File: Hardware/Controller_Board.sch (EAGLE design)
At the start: 19 parts, among them Q7 3.6864MHz, U1 ATMEGA328P-PU, U2 REF3020AIDBZT

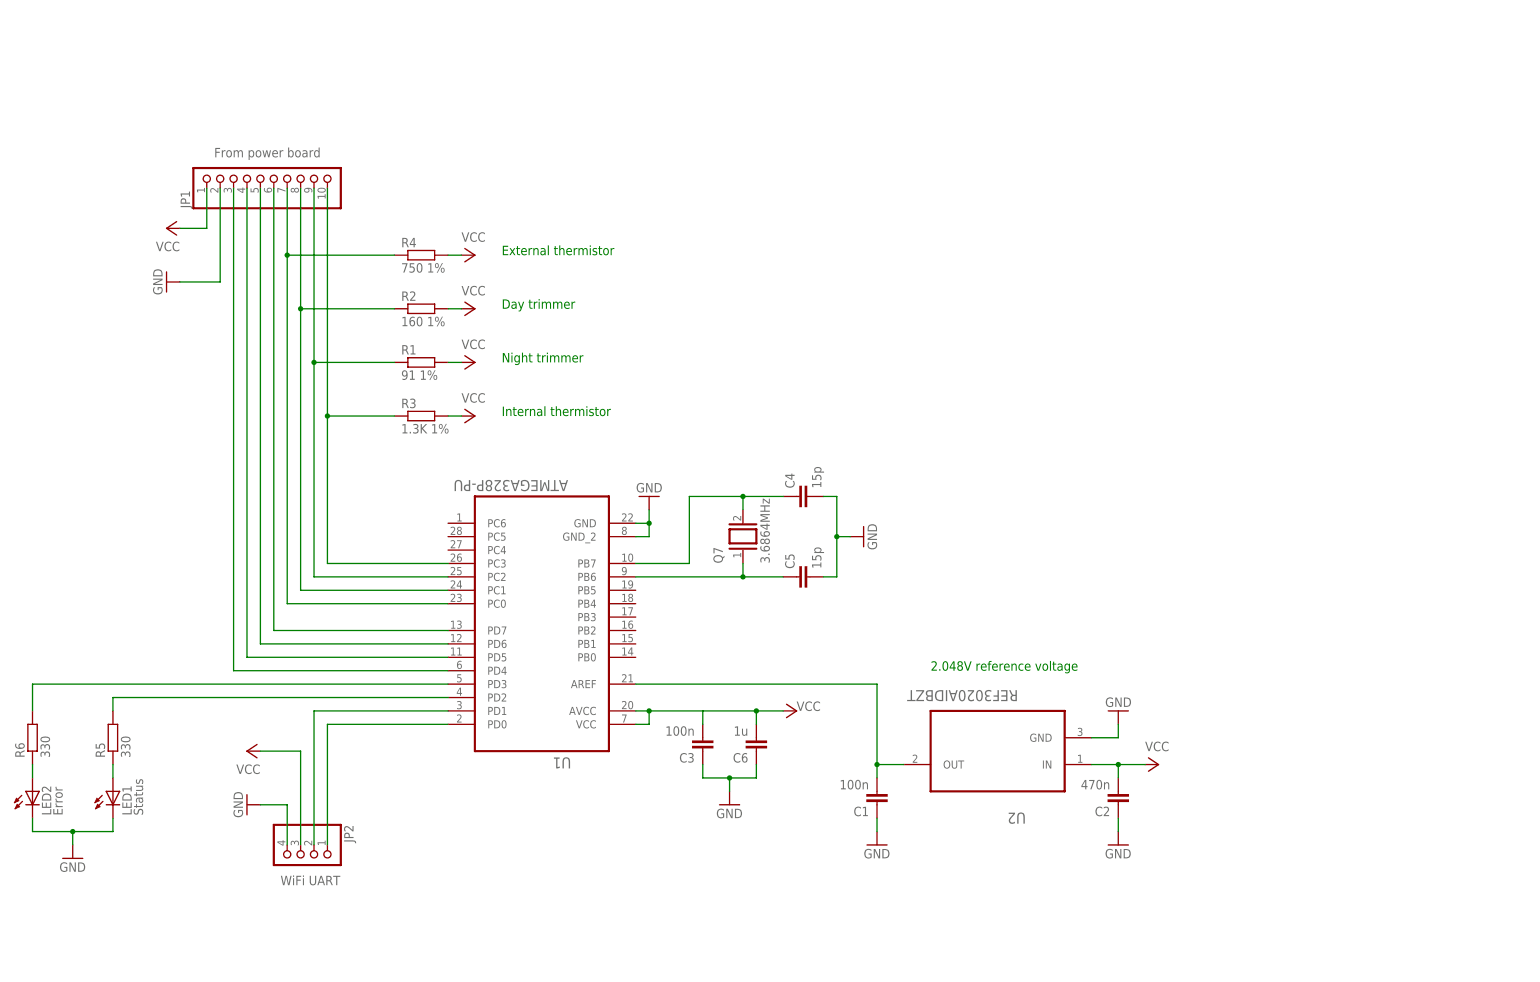
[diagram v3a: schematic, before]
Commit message: Added spare leds and connector to the controller board. Components could be populated if needed.
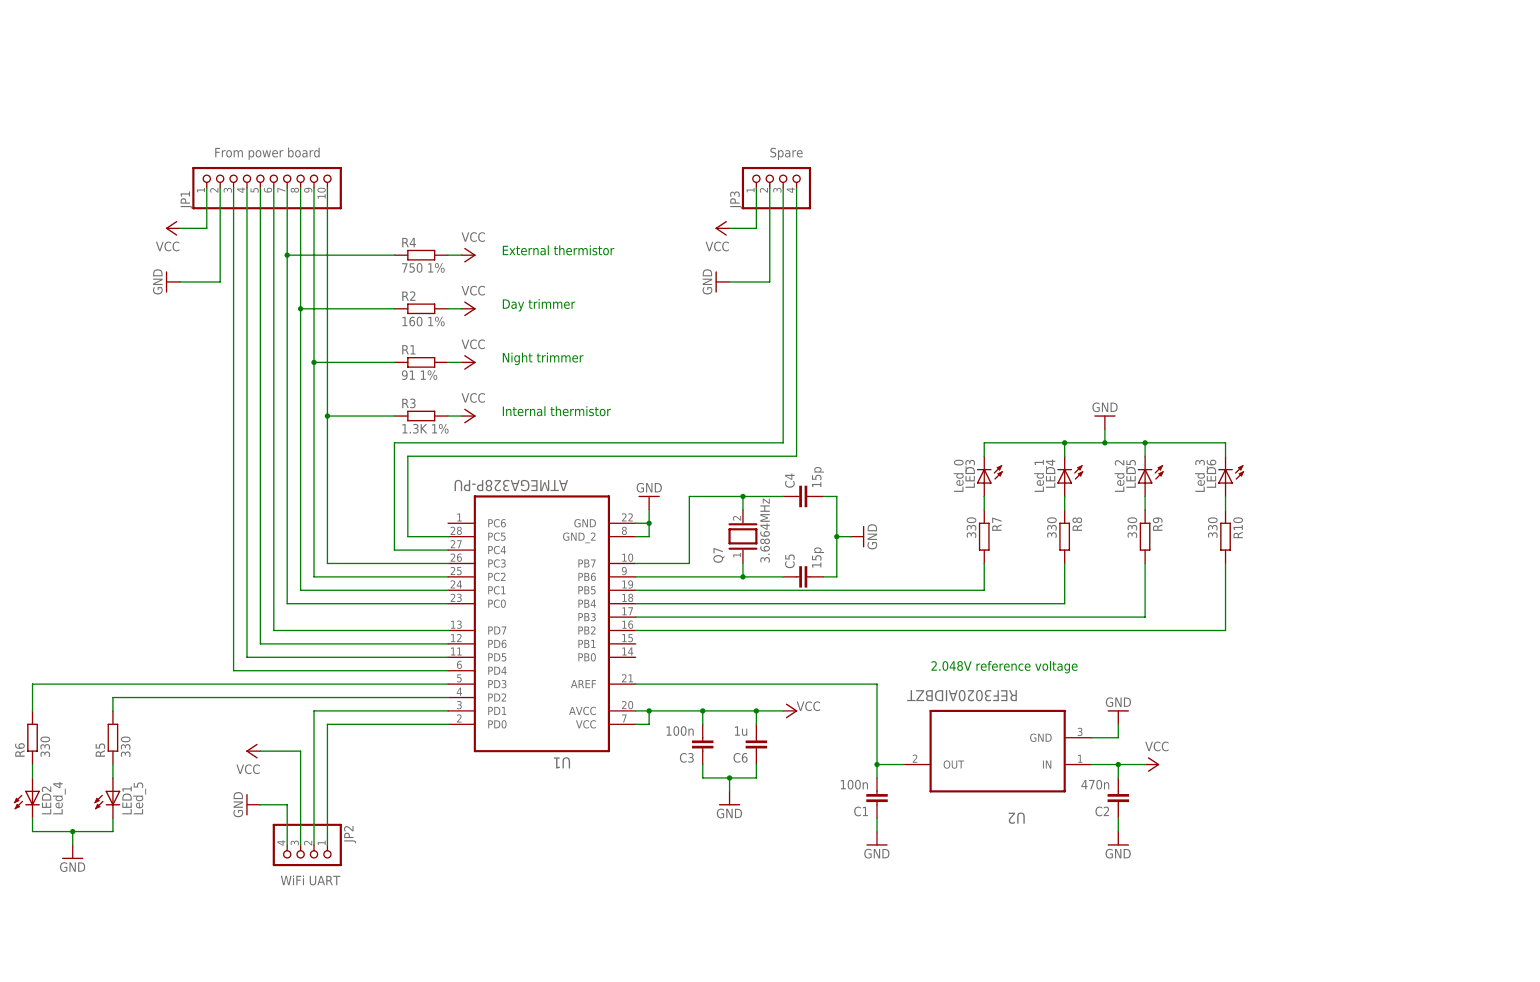
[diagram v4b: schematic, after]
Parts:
- added JP3: Spare, pinhead:PINHD-1X4
- added LED3: Led_0, led:LED5MM
- added LED4: Led_1, led:LED5MM
- added LED5: Led_2, led:LED5MM
- added LED6: Led_3, led:LED5MM
- added R10, R7, R8, R9: 330, resistor:R-EU_0207/10
- LED1: value Status -> Led_5
- LED2: value Error -> Led_4
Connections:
- new net N$15: LED3.A, R7.1
- new net N$17: LED4.A, R8.1
- new net N$18: R8.2, U1.PB4
- new net N$19: R7.2, U1.PB5
- new net N$20: JP3.3, U1.PC4
- new net N$21: LED5.A, R9.1
- new net N$22: R9.2, U1.PB3
- new net N$23: JP3.4, U1.PC5
- new net N$24: LED6.A, R10.1
- new net N$25: R10.2, U1.PB2
- net GND: now also JP3.2, LED3.C, LED4.C, LED5.C, LED6.C
- net VCC: now also JP3.1
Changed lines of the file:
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@@
 <setting verticaltext="down"/>
 </settings>
-<grid distance="0.1" unitdist="inch" unit="inch" style="dots" multiple="1" display="yes" altdistance="0.01" altunitdist="inch" altunit="inch"/>
+<grid distance="0.1" unitdist="inch" unit="inch" style="lines" multiple="1" display="yes" altdistance="0.01" altunitdist="inch" altunit="inch"/>
 <layers>
 <layer number="1" name="Top" color="4" fill="1" visible="no" active="no"/>
@@
 <part name="GND2" library="supply1" deviceset="GND" device=""/>
 <part name="P+7" library="supply1" deviceset="VCC" device=""/>
-<part name="LED1" library="led" deviceset="LED" device="5MM" value="Status"/>
+<part name="LED1" library="led" deviceset="LED" device="5MM" value="Led_5"/>
 <part name="GND3" library="supply1" deviceset="GND" device=""/>
 <part name="R5" library="resistor" deviceset="R-EU_" device="0207/10" value="330"/>
 <part name="C6" library="rcl" deviceset="C-EU" device="050-035X075" value="1u"/>
-<part name="LED2" library="led" deviceset="LED" device="5MM" value="Error"/>
+<part name="LED2" library="led" deviceset="LED" device="5MM" value="Led_4"/>
 <part name="R6" library="resistor" deviceset="R-EU_" device="0207/10" value="330"/>
+<part name="LED3" library="led" deviceset="LED" device="5MM" value="Led_0"/>
+<part name="GND5" library="supply1" deviceset="GND" device=""/>
+<part name="R7" library="resistor" deviceset="R-EU_" device="0207/10" value="330"/>
+<part name="LED4" library="led" deviceset="LED" device="5MM" value="Led_1"/>
+<part name="R8" library="resistor" deviceset="R-EU_" device="0207/10" value="330"/>
+<part name="LED5" library="led" deviceset="LED" device="5MM" value="Led_2"/>
+<part name="R9" library="resistor" deviceset="R-EU_" device="0207/10" value="330"/>
+<part name="LED6" library="led" deviceset="LED" device="5MM" value="Led_3"/>
+<part name="R10" library="resistor" deviceset="R-EU_" device="0207/10" value="330"/>
+<part name="JP3" library="pinhead" deviceset="PINHD-1X4" device="" value="Spare"/>
+<part name="P+8" library="supply1" deviceset="VCC" device=""/>
+<part name="GND7" library="supply1" deviceset="GND" device=""/>
 </parts>
 <sheets>
@@
 <instance part="LED2" gate="G$1" x="-43.18" y="127"/>
 <instance part="R6" gate="G$1" x="-43.18" y="137.16" rot="R90"/>
+<instance part="LED3" gate="G$1" x="137.16" y="185.42" rot="R180"/>
+<instance part="GND5" gate="1" x="160.02" y="198.12" rot="R180"/>
+<instance part="R7" gate="G$1" x="137.16" y="175.26" rot="R270"/>
+<instance part="LED4" gate="G$1" x="152.4" y="185.42" rot="R180"/>
+<instance part="R8" gate="G$1" x="152.4" y="175.26" rot="R270"/>
+<instance part="LED5" gate="G$1" x="167.64" y="185.42" rot="R180"/>
+<instance part="R9" gate="G$1" x="167.64" y="175.26" rot="R270"/>
+<instance part="LED6" gate="G$1" x="182.88" y="185.42" rot="R180"/>
+<instance part="R10" gate="G$1" x="182.88" y="175.26" rot="R270"/>
+<instance part="JP3" gate="A" x="99.06" y="243.84" smashed="yes" rot="R90">
+<attribute name="NAME" x="90.805" y="237.49" size="1.778" layer="95" rot="R90"/>
+<attribute name="VALUE" x="102.87" y="248.92" size="1.778" layer="96" rot="R180"/>
+</instance>
+<instance part="P+8" gate="VCC" x="86.36" y="233.68" rot="R90"/>
+<instance part="GND7" gate="1" x="86.36" y="223.52" rot="R270"/>
 </instances>
 <busses>
@@
 <junction x="-35.56" y="119.38"/>
 </segment>
+<segment>
+<pinref part="LED5" gate="G$1" pin="C"/>
+<wire x1="167.64" y1="190.5" x2="167.64" y2="193.04" width="0.1524" layer="91"/>
+<wire x1="167.64" y1="193.04" x2="160.02" y2="193.04" width="0.1524" layer="91"/>
+<pinref part="GND5" gate="1" pin="GND"/>
+<wire x1="160.02" y1="193.04" x2="152.4" y2="193.04" width="0.1524" layer="91"/>
+<wire x1="160.02" y1="195.58" x2="160.02" y2="193.04" width="0.1524" layer="91"/>
+<pinref part="LED4" gate="G$1" pin="C"/>
+<wire x1="152.4" y1="190.5" x2="152.4" y2="193.04" width="0.1524" layer="91"/>
+<pinref part="LED3" gate="G$1" pin="C"/>
+<wire x1="152.4" y1="193.04" x2="137.16" y2="193.04" width="0.1524" layer="91"/>
+<wire x1="137.16" y1="193.04" x2="137.16" y2="190.5" width="0.1524" layer="91"/>
+<junction x="152.4" y="193.04"/>
+<junction x="160.02" y="193.04"/>
+<pinref part="LED6" gate="G$1" pin="C"/>
+<wire x1="182.88" y1="190.5" x2="182.88" y2="193.04" width="0.1524" layer="91"/>
+<wire x1="182.88" y1="193.04" x2="167.64" y2="193.04" width="0.1524" layer="91"/>
+<junction x="167.64" y="193.04"/>
+</segment>
+<segment>
+<pinref part="GND7" gate="1" pin="GND"/>
+<wire x1="88.9" y1="223.52" x2="96.52" y2="223.52" width="0.1524" layer="91"/>
+<pinref part="JP3" gate="A" pin="2"/>
+<wire x1="96.52" y1="223.52" x2="96.52" y2="241.3" width="0.1524" layer="91"/>
+</segment>
 </net>
 <net name="VCC" class="0">
@@
 </segment>
 <segment>
-<pinref part="U2" gate="A" pin="IN"/>
-<wire x1="157.48" y1="132.08" x2="162.56" y2="132.08" width="0.1524" layer="91"/>
 <pinref part="C2" gate="G$1" pin="2"/>
 <wire x1="162.56" y1="132.08" x2="162.56" y2="129.54" width="0.1524" layer="91"/>
-<junction x="162.56" y="132.08"/>
 <wire x1="162.56" y1="132.08" x2="167.64" y2="132.08" width="0.1524" layer="91"/>
 <pinref part="P+4" gate="VCC" pin="VCC"/>
+<pinref part="U2" gate="A" pin="IN"/>
+<wire x1="162.56" y1="132.08" x2="157.48" y2="132.08" width="0.1524" layer="91"/>
+<junction x="162.56" y="132.08"/>
 </segment>
 <segment>
@@
 <wire x1="83.82" y1="142.24" x2="73.66" y2="142.24" width="0.1524" layer="91"/>
 <junction x="73.66" y="142.24"/>
+<junction x="83.82" y="142.24"/>
 </segment>
 <segment>
@@
 <wire x1="0" y1="134.62" x2="7.62" y2="134.62" width="0.1524" layer="91"/>
 <wire x1="7.62" y1="134.62" x2="7.62" y2="116.84" width="0.1524" layer="91"/>
+</segment>
+<segment>
+<pinref part="P+8" gate="VCC" pin="VCC"/>
+<wire x1="88.9" y1="233.68" x2="93.98" y2="233.68" width="0.1524" layer="91"/>
+<pinref part="JP3" gate="A" pin="1"/>
+<wire x1="93.98" y1="233.68" x2="93.98" y2="241.3" width="0.1524" layer="91"/>
 </segment>
 </net>
@@
 </segment>
 </net>
+<net name="N$15" class="0">
+<segment>
+<pinref part="R7" gate="G$1" pin="1"/>
+<pinref part="LED3" gate="G$1" pin="A"/>
+<wire x1="137.16" y1="180.34" x2="137.16" y2="182.88" width="0.1524" layer="91"/>
+</segment>
+</net>
+<net name="N$17" class="0">
+<segment>
+<pinref part="R8" gate="G$1" pin="1"/>
+<pinref part="LED4" gate="G$1" pin="A"/>
+<wire x1="152.4" y1="180.34" x2="152.4" y2="182.88" width="0.1524" layer="91"/>
+</segment>
+</net>
+<net name="N$18" class="0">
+<segment>
+<pinref part="R8" gate="G$1" pin="2"/>
+<wire x1="152.4" y1="162.56" x2="152.4" y2="170.18" width="0.1524" layer="91"/>
+<pinref part="U1" gate="A" pin="PB4"/>
+<wire x1="71.12" y1="162.56" x2="152.4" y2="162.56" width="0.1524" layer="91"/>
+</segment>
+</net>
+<net name="N$19" class="0">
+<segment>
+<pinref part="R7" gate="G$1" pin="2"/>
+<pinref part="U1" gate="A" pin="PB5"/>
+<wire x1="71.12" y1="165.1" x2="137.16" y2="165.1" width="0.1524" layer="91"/>
+<wire x1="137.16" y1="165.1" x2="137.16" y2="170.18" width="0.1524" layer="91"/>
+</segment>
+</net>
+<net name="N$21" class="0">
+<segment>
+<pinref part="R9" gate="G$1" pin="1"/>
+<pinref part="LED5" gate="G$1" pin="A"/>
+<wire x1="167.64" y1="180.34" x2="167.64" y2="182.88" width="0.1524" layer="91"/>
+</segment>
+</net>
+<net name="N$22" class="0">
+<segment>
+<pinref part="R9" gate="G$1" pin="2"/>
+<pinref part="U1" gate="A" pin="PB3"/>
+<wire x1="71.12" y1="160.02" x2="167.64" y2="160.02" width="0.1524" layer="91"/>
+<wire x1="167.64" y1="160.02" x2="167.64" y2="170.18" width="0.1524" layer="91"/>
+</segment>
+</net>
+<net name="N$24" class="0">
+<segment>
+<pinref part="R10" gate="G$1" pin="1"/>
+<pinref part="LED6" gate="G$1" pin="A"/>
+<wire x1="182.88" y1="180.34" x2="182.88" y2="182.88" width="0.1524" layer="91"/>
+</segment>
+</net>
+<net name="N$25" class="0">
+<segment>
+<pinref part="R10" gate="G$1" pin="2"/>
+<pinref part="U1" gate="A" pin="PB2"/>
+<wire x1="71.12" y1="157.48" x2="182.88" y2="157.48" width="0.1524" layer="91"/>
+<wire x1="182.88" y1="157.48" x2="182.88" y2="170.18" width="0.1524" layer="91"/>
+</segment>
+</net>
+<net name="N$20" class="0">
+<segment>
+<pinref part="JP3" gate="A" pin="3"/>
+<wire x1="99.06" y1="241.3" x2="99.06" y2="193.04" width="0.1524" layer="91"/>
+<wire x1="99.06" y1="193.04" x2="25.4" y2="193.04" width="0.1524" layer="91"/>
+<wire x1="25.4" y1="193.04" x2="25.4" y2="172.72" width="0.1524" layer="91"/>
+<pinref part="U1" gate="A" pin="PC4"/>
+<wire x1="25.4" y1="172.72" x2="35.56" y2="172.72" width="0.1524" layer="91"/>
+</segment>
+</net>
+<net name="N$23" class="0">
+<segment>
+<pinref part="U1" gate="A" pin="PC5"/>
+<wire x1="35.56" y1="175.26" x2="27.94" y2="175.26" width="0.1524" layer="91"/>
+<wire x1="27.94" y1="175.26" x2="27.94" y2="190.5" width="0.1524" layer="91"/>
+<wire x1="27.94" y1="190.5" x2="101.6" y2="190.5" width="0.1524" layer="91"/>
+<pinref part="JP3" gate="A" pin="4"/>
+<wire x1="101.6" y1="190.5" x2="101.6" y2="241.3" width="0.1524" layer="91"/>
+</segment>
+</net>

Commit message: Added microcontroller SPI programming header to the controller board.
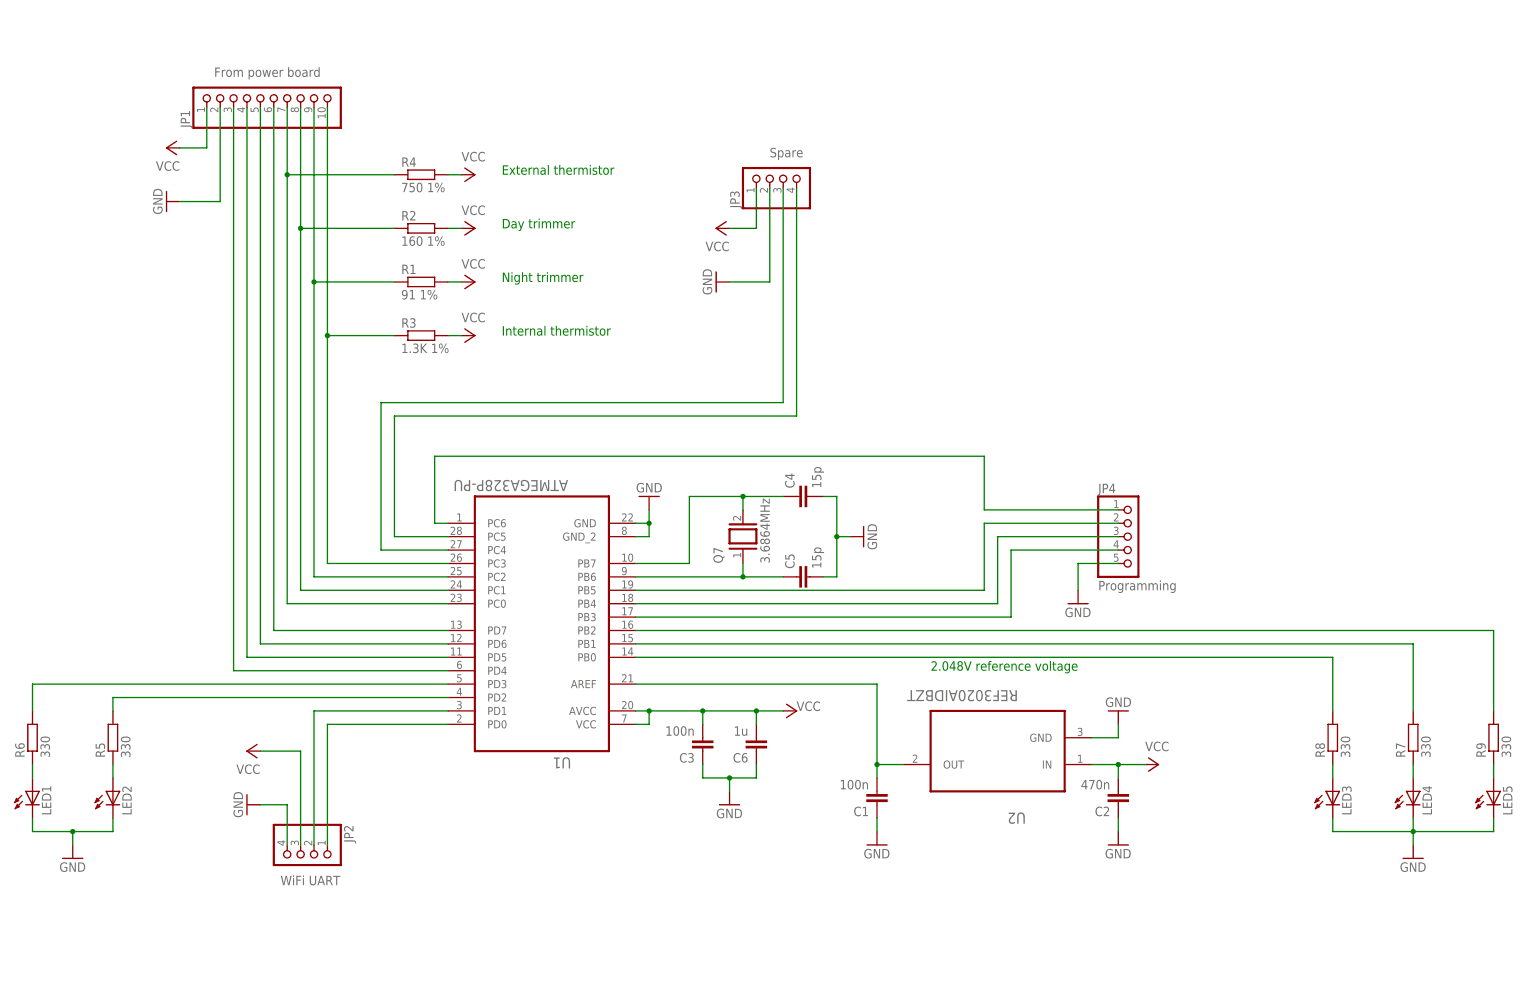
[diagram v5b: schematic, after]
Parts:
- removed LED6: Led_3, led:LED5MM
- removed R10: 330, resistor:R-EU_0207/10
- added JP4: Programming, pinhead:PINHD-1X5
- LED1: value Led_5 -> (none)
- LED2: value Led_4 -> (none)
- LED3: value Led_0 -> (none)
- LED4: value Led_1 -> (none)
- LED5: value Led_2 -> (none)
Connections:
- new net N$21: LED4.A, R7.1
- new net N$28: R9.2, U1.PB2
- net GND: now also JP4.5; no longer LED6.C
- net N$11: now also LED1.A; no longer LED2.A
- net N$12: now also LED2.A; no longer LED1.A
- net N$15: now also JP4.2, U1.PB5; no longer LED3.A, R7.1
- net N$17: now also JP4.3, U1.PB4; no longer LED4.A, R8.1
- net N$18: now also JP4.4, U1.PB3; no longer R8.2, U1.PB4
- net N$19: now also JP4.1, U1.PC6; no longer R7.2, U1.PB5
- net N$22: now also LED3.A, R8.1; no longer R9.2, U1.PB3
- net N$24: now also R8.2, U1.PB0; no longer LED6.A, R10.1
- net N$25: now also R7.2, U1.PB1; no longer R10.2, U1.PB2
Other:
- moved on the sheet: JP1, LED1, LED2, LED3, LED4, LED5, R1, R2, R3, R4, R7, R8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
